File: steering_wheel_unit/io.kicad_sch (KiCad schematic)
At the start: 45 parts, among them U5 SN65HVD232

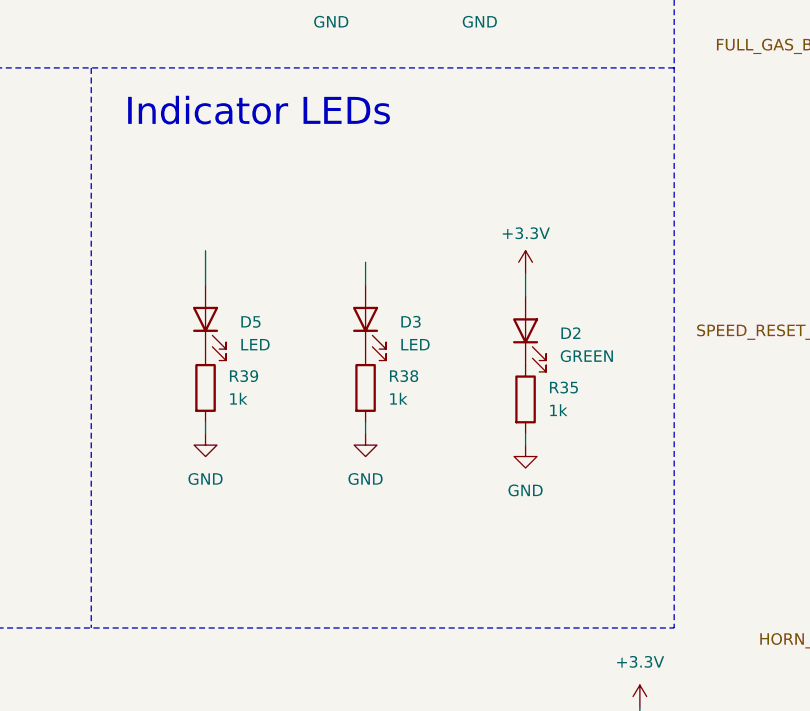
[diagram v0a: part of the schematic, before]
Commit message: Add jtag socket and main connector, missing footprints and 3d models
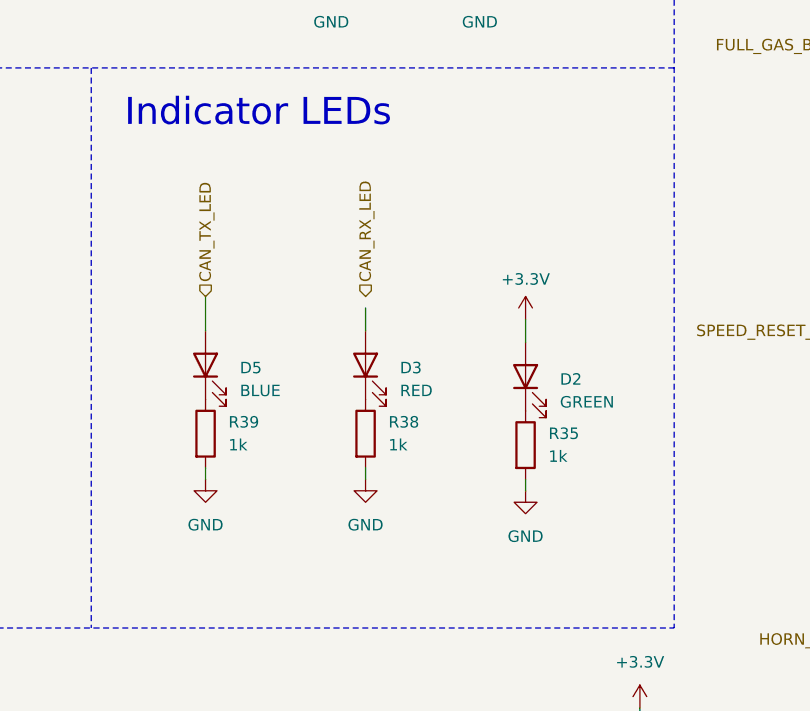
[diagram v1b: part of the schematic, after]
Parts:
- D3: value LED -> RED
- D5: value LED -> BLUE
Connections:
- net CAN_TX_LED: now reaches D5.2 (A)
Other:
- moved on the sheet: D2, D3, D5, R35, R38, R39
